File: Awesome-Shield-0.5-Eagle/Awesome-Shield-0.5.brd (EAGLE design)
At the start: 100 x 80 mm, 24 parts, among them J1 ARDUINO_R3_SHIELDUNO_R3_SHIEL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, SW1 SPST_TACT-EVQQ2

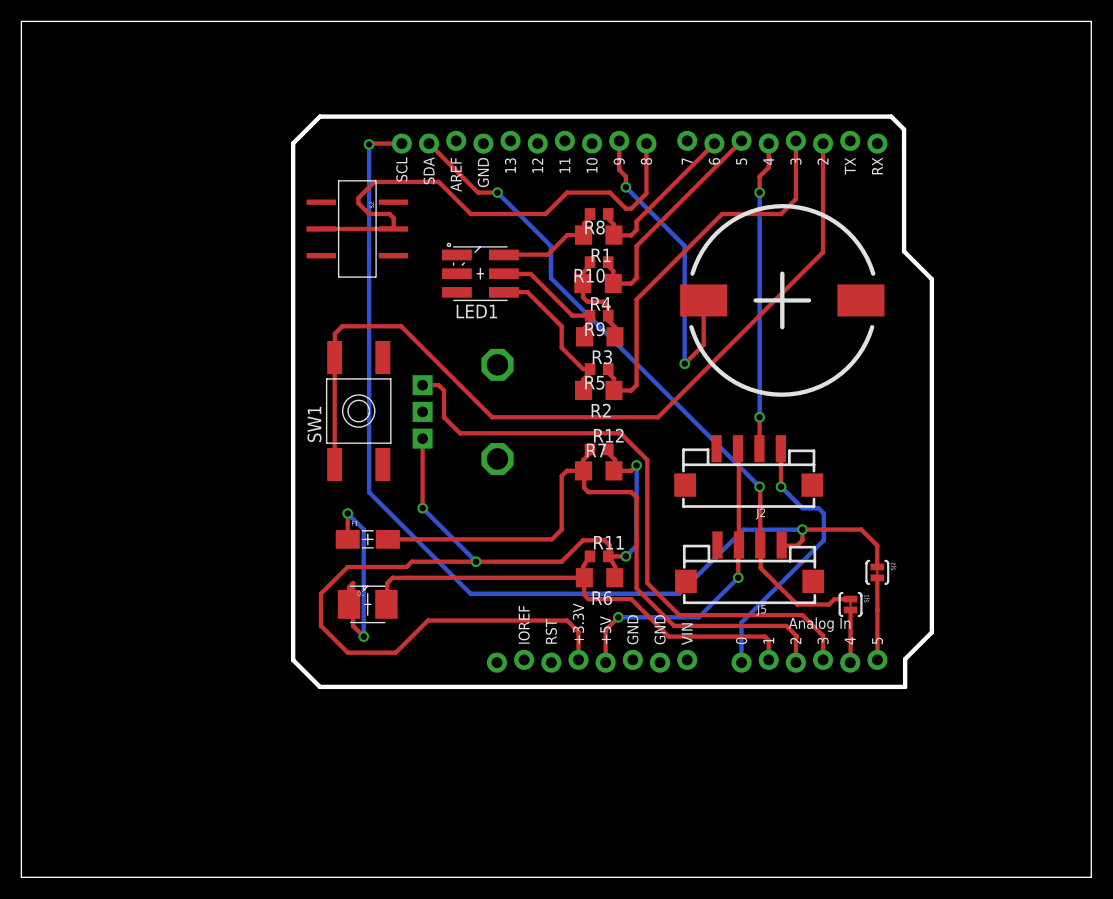
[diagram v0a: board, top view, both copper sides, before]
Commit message: updated component locations and traces for better UX
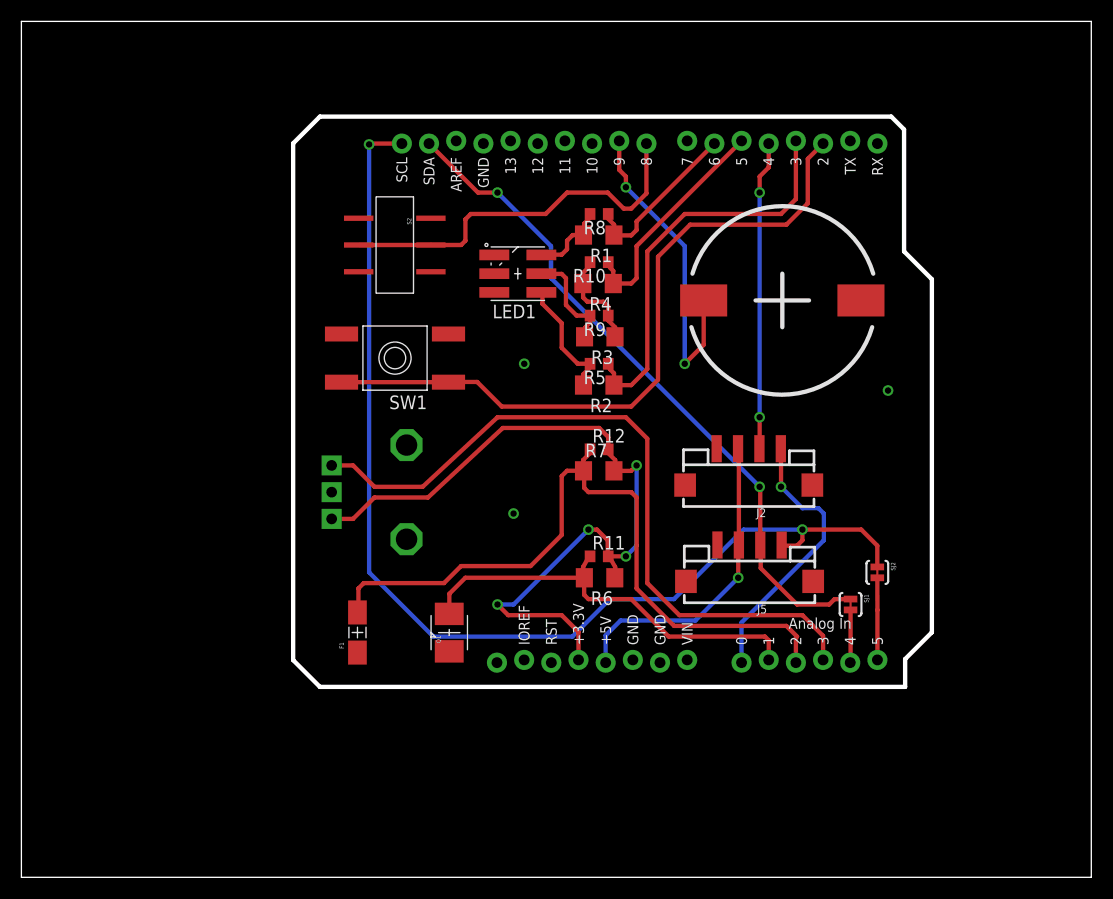
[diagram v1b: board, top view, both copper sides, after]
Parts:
- moved RV1 11.3 mm to (36.0, 36.0)
- moved F1 8.76 mm to (31.4, 22.9), turned to 90 degrees
- moved Q1 8.06 mm to (40.0, 22.9), turned to 0 degrees
- moved SW1 6.00 mm to (34.9, 48.5), turned to 180 degrees
- moved S2 3.81 mm to (34.9, 59.1)
- moved LED1 3.50 mm to (46.4, 56.4)
- moved R2 0.50 mm to (54.0, 46.0)
- moved R5 0.50 mm to (54.0, 48.0)
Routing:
- net GND: track 22.1 -> 0.00 mm, vias 2 -> 3
- net +3V3: track 94.0 -> 74.8 mm
- net D2: track 78.3 -> 65.3 mm
- net D8: track 47.6 -> 36.0 mm
- net A3: track 57.6 -> 67.9 mm
- net SCL: track 95.4 -> 103.1 mm
- net A2: track 60.9 -> 68.1 mm
- net A1: track 46.3 -> 40.1 mm
- net N$8: track 10.4 -> 7.40 mm
- net N$9: track 14.5 -> 11.5 mm
- net N$3: track 11.9 -> 9.83 mm
- net D3: track 36.8 -> 38.3 mm
- net +5V: track 29.6 -> 29.3 mm, vias 2 -> 1

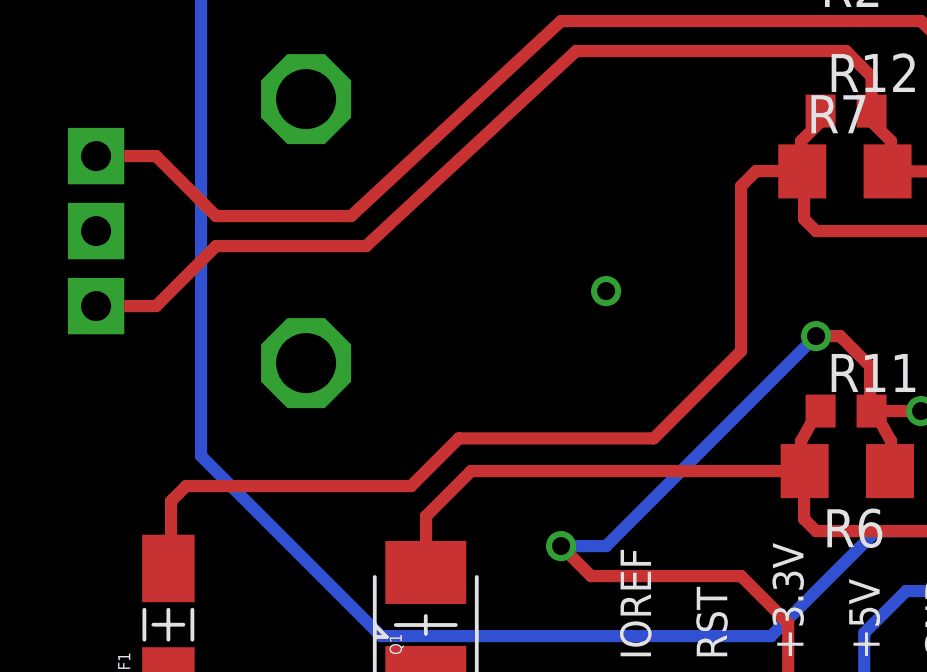
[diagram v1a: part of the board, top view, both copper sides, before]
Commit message: trace tweaks for better ground pour covereage
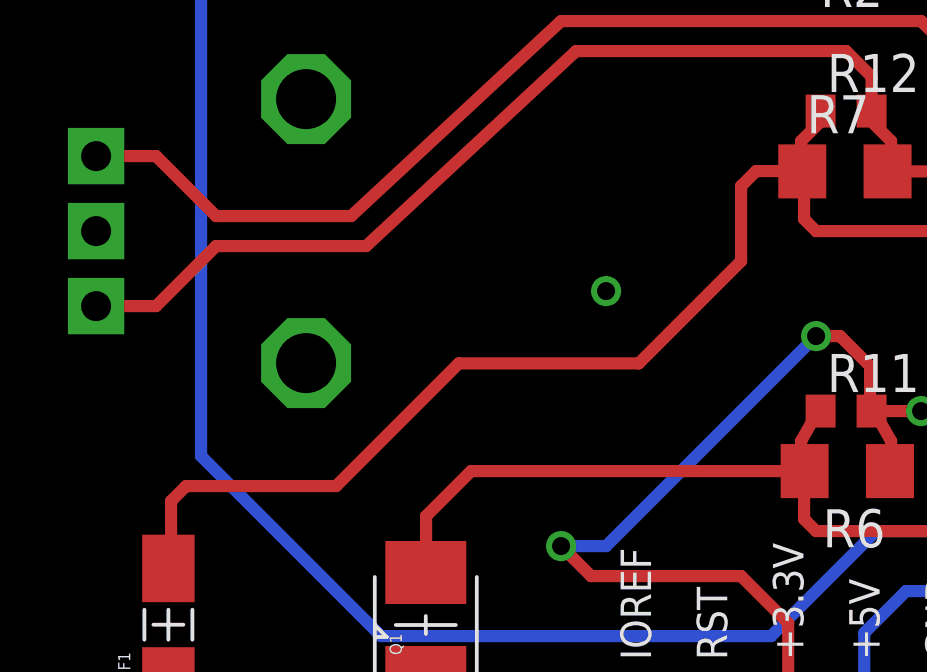
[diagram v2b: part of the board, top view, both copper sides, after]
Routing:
- net A2: track 68.1 -> 66.4 mm
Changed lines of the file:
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@@
 <wire x1="52.6" y1="36.4" x2="52.6" y2="37.928" width="0.4064" layer="1"/>
 <wire x1="52.6" y1="37.928" x2="52.538" y2="37.99" width="0.4064" layer="1"/>
-<wire x1="47.59" y1="29.09" x2="50.5" y2="32" width="0.4064" layer="1"/>
-<wire x1="50.5" y1="32" x2="50.5" y2="37.5" width="0.4064" layer="1"/>
+<wire x1="47.09" y1="31.59" x2="50.5" y2="35" width="0.4064" layer="1"/>
+<wire x1="50.5" y1="35" x2="50.5" y2="37.5" width="0.4064" layer="1"/>
 <wire x1="50.5" y1="37.5" x2="51" y2="38" width="0.4064" layer="1"/>
 <wire x1="51" y1="38" x2="52.528" y2="38" width="0.4064" layer="1"/>
@@
 <wire x1="57" y1="36" x2="57.5" y2="35.5" width="0.4064" layer="1"/>
 <wire x1="57.5" y1="35.5" x2="57.5" y2="27" width="0.4064" layer="1"/>
-<wire x1="47.59" y1="29.09" x2="41.09" y2="29.09" width="0.4064" layer="1"/>
-<wire x1="41.09" y1="29.09" x2="39.5" y2="27.5" width="0.4064" layer="1"/>
-<wire x1="39.5" y1="27.5" x2="32" y2="27.5" width="0.4064" layer="1"/>
+<wire x1="47.09" y1="31.59" x2="41.09" y2="31.59" width="0.4064" layer="1"/>
+<wire x1="41.09" y1="31.59" x2="37" y2="27.5" width="0.4064" layer="1"/>
+<wire x1="37" y1="27.5" x2="32" y2="27.5" width="0.4064" layer="1"/>
 <wire x1="32" y1="27.5" x2="31.5" y2="27" width="0.4064" layer="1"/>
 <wire x1="31.5" y1="27" x2="31.5" y2="24.845" width="0.4064" layer="1"/>

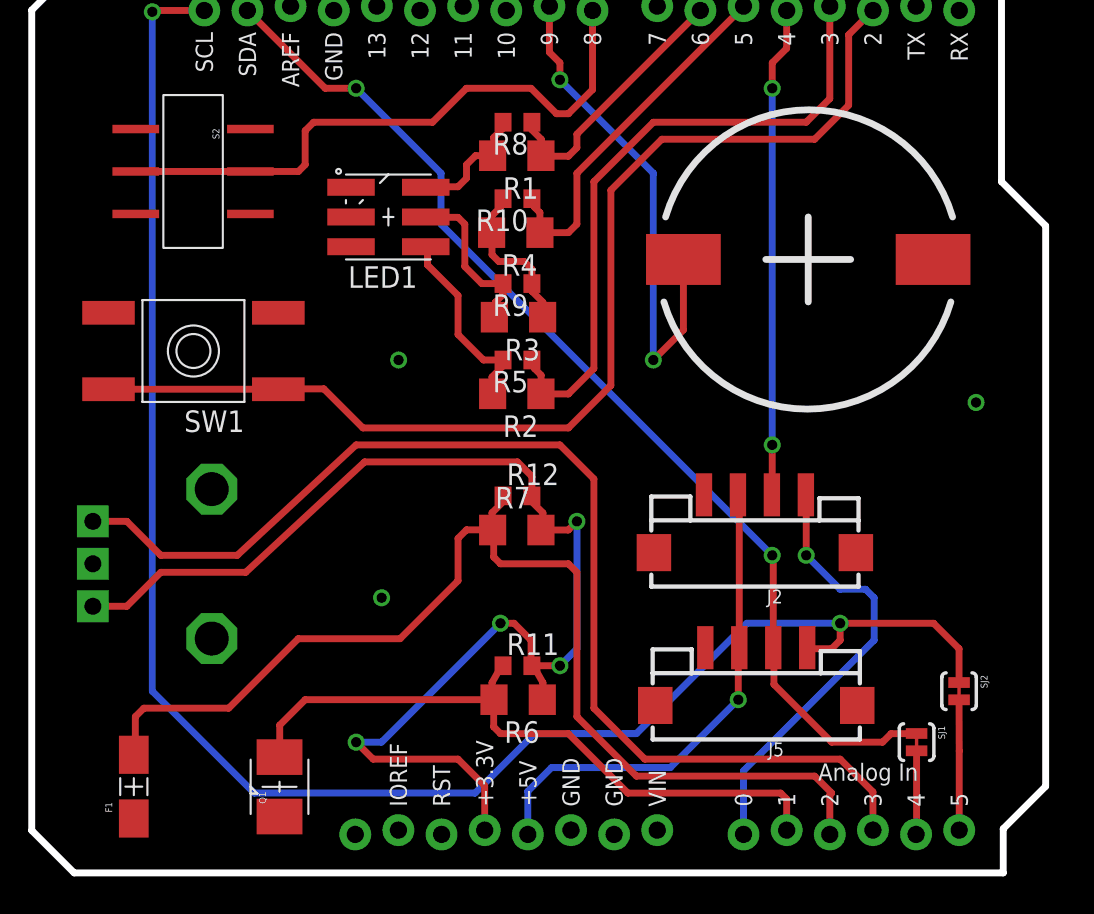
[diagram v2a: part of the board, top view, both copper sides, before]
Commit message: fixed silkscreen to comply with DRC
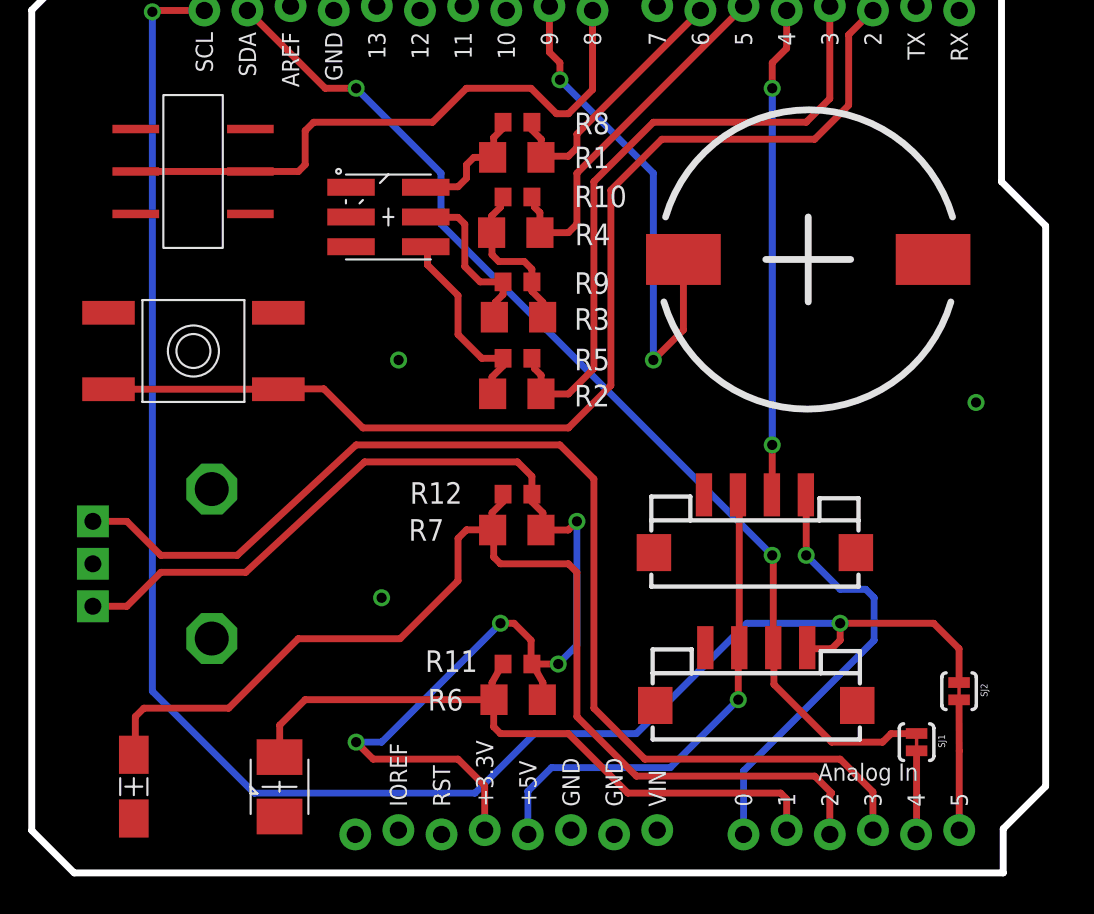
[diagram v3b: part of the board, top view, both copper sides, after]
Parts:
- moved R1 0.10 mm to (54.0, 59.9)
- moved R10 0.10 mm to (54.0, 57.6)
- moved R11 0.10 mm to (54.0, 30.1)
- moved R12 0.10 mm to (54.0, 40.1)
- moved R5 0.10 mm to (54.0, 48.1)
- moved R9 0.10 mm to (54.0, 52.6)
